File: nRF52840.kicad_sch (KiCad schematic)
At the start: 20 parts, among them J3 JTAG_TC2030, J4 RGB, Q2 2N7002, Q3 AO3407, SW29 RESET, U4 MS88SF3

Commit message: feat(pcb): Version 0.3.1
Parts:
- U4: value MS88SF3 -> (none); footprint Conejo:MS88SF3_PeteJohanson -> (none)
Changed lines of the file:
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@@
     (in_bom yes) (on_board yes)
     (property "Reference" "U4" (id 0) (at 142.875 125.7331 0))
-    (property "Value" "MS88SF3" (id 1) (at 142.875 128.27 0))
-    (property "Footprint" "Conejo:MS88SF3_PeteJohanson" (id 2) (at 170.815 179.07 0)
+    (property "Value" "" (id 1) (at 142.875 128.27 0))
+    (property "Footprint" "" (id 2) (at 170.815 179.07 0)
       (effects (font (size 1.27 1.27)) hide)
     )
@@
       (effects (font (size 1.27 1.27)) (justify left))
     )
-    (property "Value" "MS88SF3" (id 1) (at 161.29 97.155 0)
+    (property "Value" "" (id 1) (at 161.29 97.155 0)
       (effects (font (size 1.27 1.27)) (justify left))
     )
-    (property "Footprint" "Conejo:MS88SF3_PeteJohanson" (id 2) (at 170.815 100.33 0)
+    (property "Footprint" "" (id 2) (at 170.815 100.33 0)
       (effects (font (size 1.27 1.27)) hide)
     )

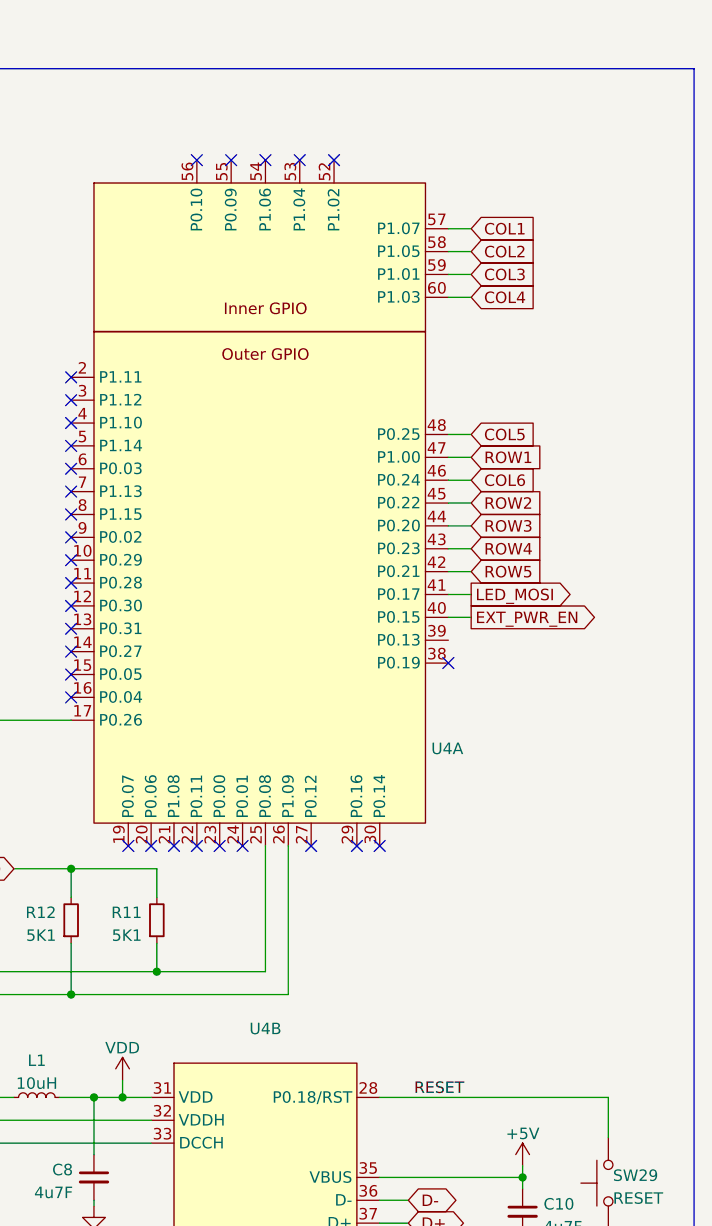
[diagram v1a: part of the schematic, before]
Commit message: feat(pcb): Version 0.3.2
- Move TC2030 footprint to accessible location
- Move diodes to be outside of 14mmx14mm switch area
- Update BOM to remove footprints that don't require placement
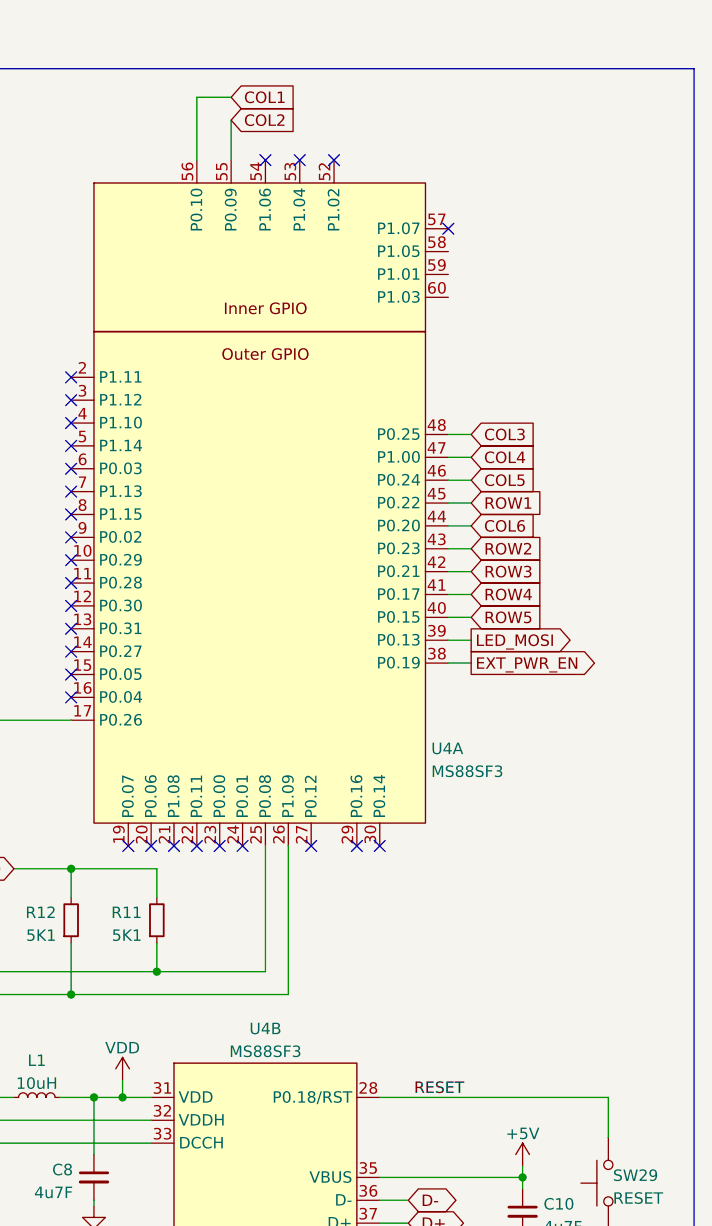
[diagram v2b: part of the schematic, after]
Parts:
- U4: value (none) -> MS88SF3; footprint (none) -> Conejo:MS88SF3_V2
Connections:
- net COL1: now also U4.56 (P0.10); no longer U4.57 (P1.07)
- net COL2: now also U4.55 (P0.09); no longer U4.58 (P1.05)
- net COL3: now also U4.48 (P0.25); no longer U4.59 (P1.01)
- net COL4: now also U4.47 (P1.00); no longer U4.60 (P1.03)
- net COL5: now also U4.46 (P0.24); no longer U4.48 (P0.25)
- net COL6: now also U4.44 (P0.20); no longer U4.46 (P0.24)
- net EXT_PWR_EN: now also U4.38 (P0.19); no longer U4.40 (P0.15)
- net LED_MOSI: now also U4.39 (P0.13); no longer U4.41 (P0.17)
- net ROW1: now also U4.45 (P0.22); no longer U4.47 (P1.00)
- net ROW2: now also U4.43 (P0.23); no longer U4.45 (P0.22)
- net ROW3: now also U4.42 (P0.21); no longer U4.44 (P0.20)
- net ROW4: now also U4.41 (P0.17); no longer U4.43 (P0.23)
- net ROW5: now also U4.40 (P0.15); no longer U4.42 (P0.21)
- no-connect marks 31 -> 29

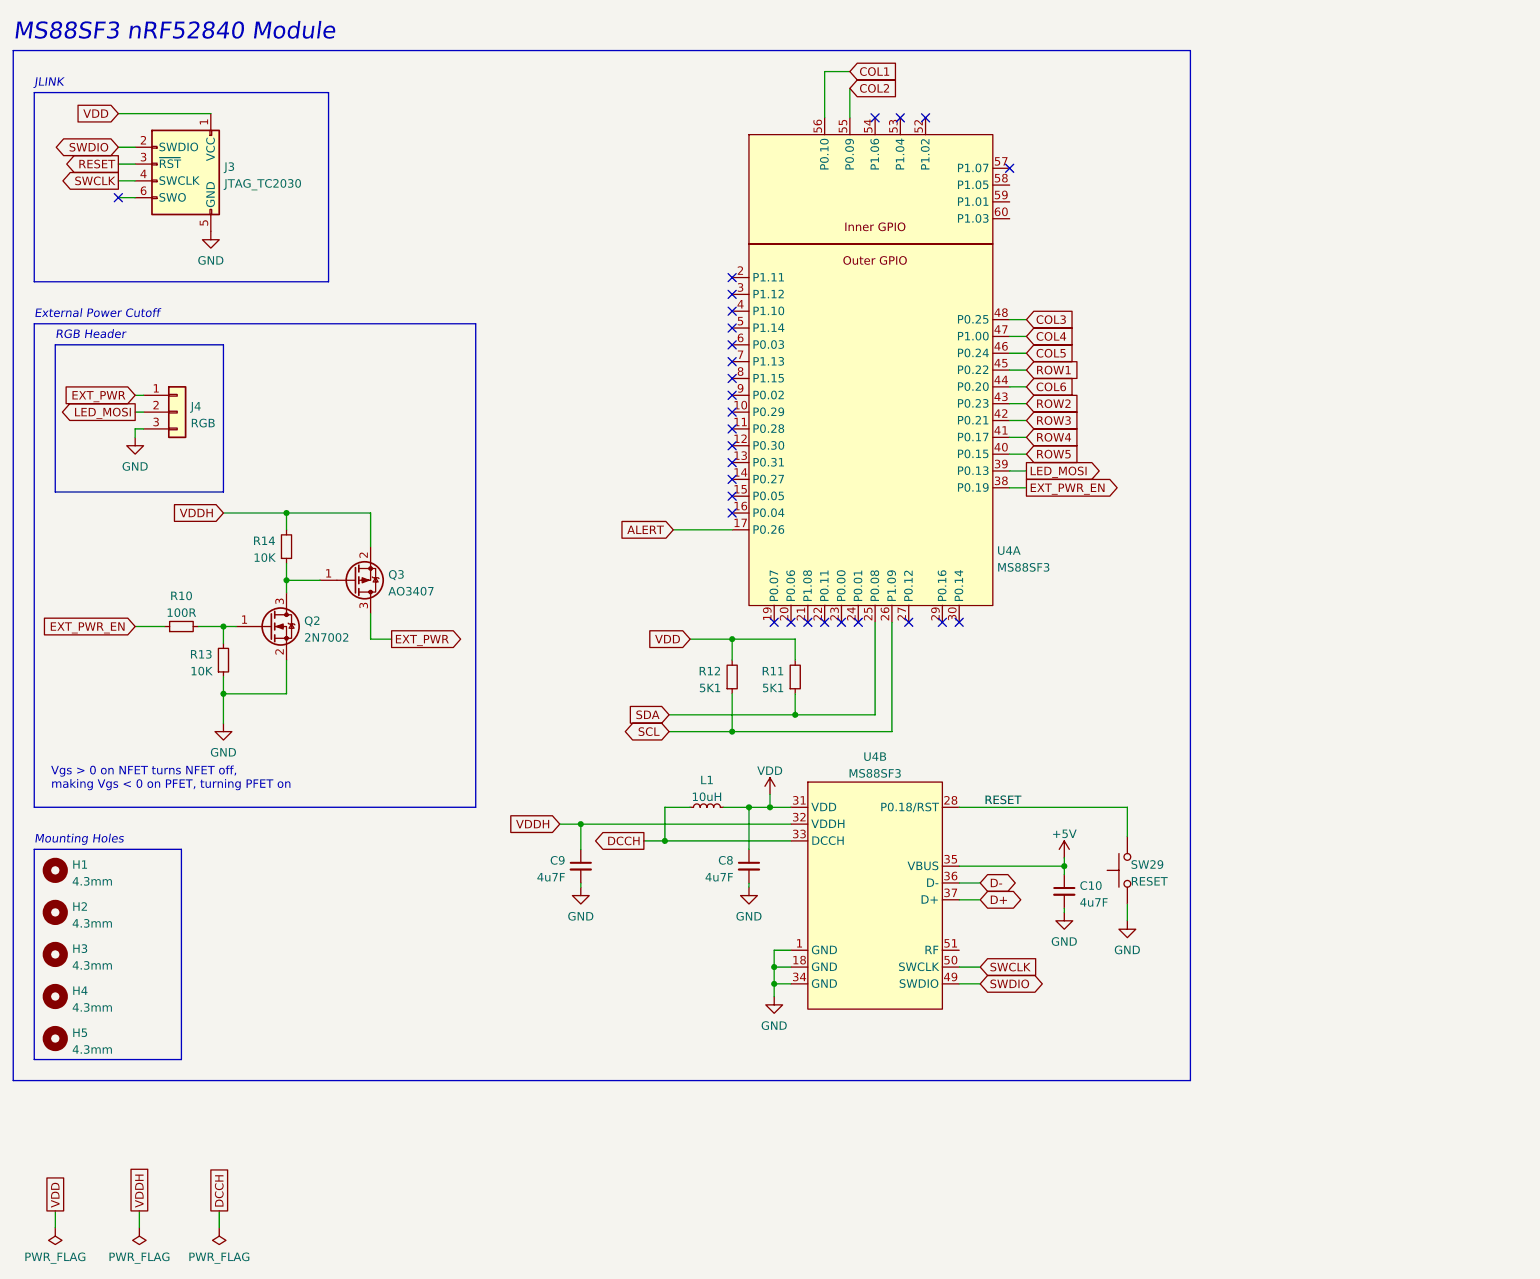
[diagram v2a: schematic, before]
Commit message: feat(schematic): Add titles and individual sheet comments
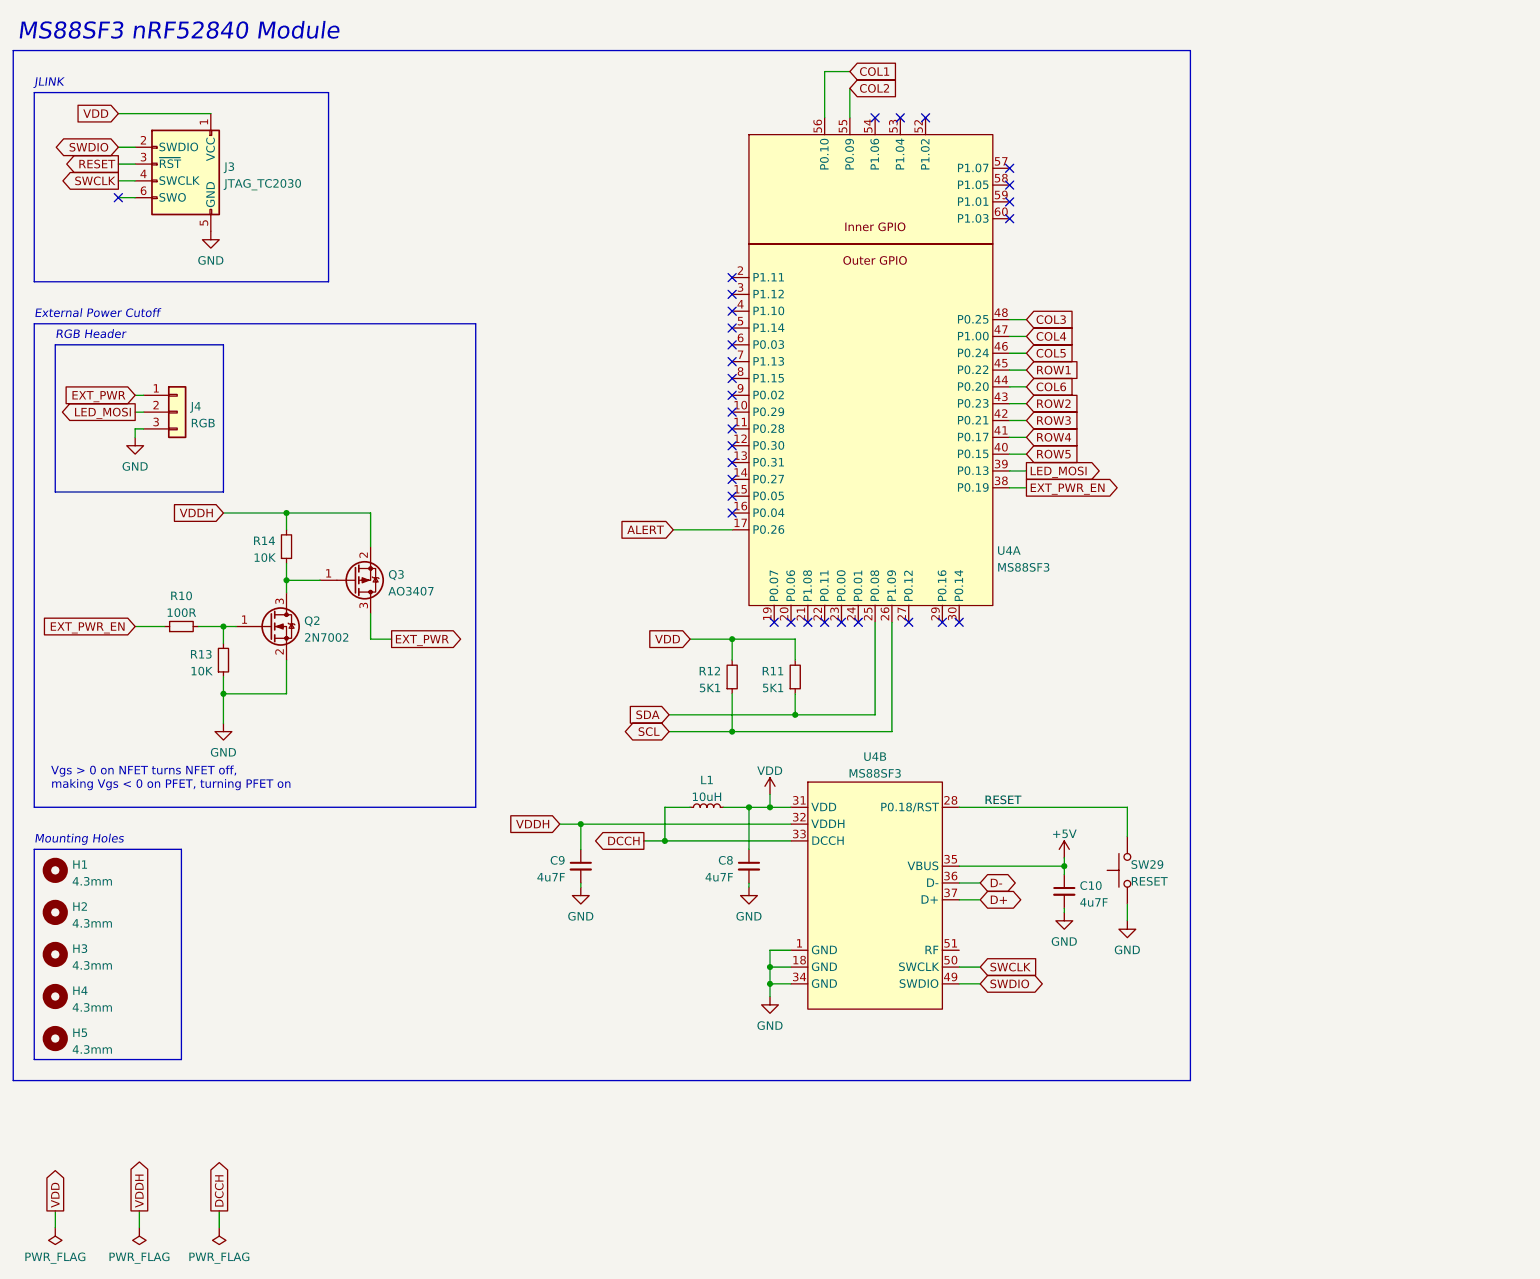
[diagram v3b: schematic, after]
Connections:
- no-connect marks 29 -> 32
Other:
- company: (none) -> Kurtis Lew
- title: (none) -> Conejo nRF52840 Keyboard - nRF52840 Module
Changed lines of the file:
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@@
 (kicad_sch (version 20211123) (generator eeschema)
   (paper "USLetter")
+  (title_block
+    (title "Conejo nRF52840 Keyboard - nRF52840 Module")
+    (company "Kurtis Lew")
+  )
   (junction (at 111.125 138.43) (diameter 0) (color 0 0 0 0)
   )
@@
   (junction (at 121.285 107.95) (diameter 0) (color 0 0 0 0)
   )
-  (junction (at 127.635 157.48) (diameter 0) (color 0 0 0 0)
+  (junction (at 127 157.48) (diameter 0) (color 0 0 0 0)
   )
   (junction (at 123.825 133.35) (diameter 0) (color 0 0 0 0)
@@
   (junction (at 127 133.35) (diameter 0) (color 0 0 0 0)
   )
-  (junction (at 127.635 160.02) (diameter 0) (color 0 0 0 0)
+  (junction (at 127 160.02) (diameter 0) (color 0 0 0 0)
   )
   (junction (at 121.285 121.92) (diameter 0) (color 0 0 0 0)
@@
   (junction (at 98.425 135.89) (diameter 0) (color 0 0 0 0)
   )
+  (no_connect (at 163.195 44.45))
   (no_connect (at 140.335 105.41))
   (no_connect (at 132.715 105.41))
@@
   (no_connect (at 121.285 86.36))
   (no_connect (at 121.285 88.9))
+  (no_connect (at 163.195 39.37))
   (no_connect (at 127.635 105.41))
   (no_connect (at 147.955 105.41))
   (no_connect (at 28.575 41.275))
+  (no_connect (at 163.195 41.91))
   (no_connect (at 155.575 105.41))
   (no_connect (at 153.035 105.41))
@@
     (stroke (width 0) (type default) (color 0 0 0 0))
   )
-  (wire (pts (xy 127.635 157.48) (xy 130.175 157.48))
+  (wire (pts (xy 127 157.48) (xy 130.175 157.48))
     (stroke (width 0) (type default) (color 0 0 0 0))
   )
@@
     (stroke (width 0) (type default) (color 0 0 0 0))
   )
-  (wire (pts (xy 127.635 157.48) (xy 127.635 160.02))
+  (wire (pts (xy 127 157.48) (xy 127 160.02))
     (stroke (width 0) (type default) (color 0 0 0 0))
   )
@@
     (stroke (width 0) (type default) (color 0 0 0 0))
   )
-  (wire (pts (xy 127.635 160.02) (xy 130.175 160.02))
+  (wire (pts (xy 127 160.02) (xy 130.175 160.02))
     (stroke (width 0) (type default) (color 0 0 0 0))
   )
@@
     (stroke (width 0) (type default) (color 0 0 0 0))
   )
-  (wire (pts (xy 127.635 161.925) (xy 127.635 160.02))
-    (stroke (width 0) (type default) (color 0 0 0 0))
-  )
-  (wire (pts (xy 127.635 154.94) (xy 127.635 157.48))
+  (wire (pts (xy 127 161.925) (xy 127 160.02))
+    (stroke (width 0) (type default) (color 0 0 0 0))
+  )
+  (wire (pts (xy 127 154.94) (xy 127 157.48))
     (stroke (width 0) (type default) (color 0 0 0 0))
   )
@@
     (stroke (width 0) (type default) (color 0 0 0 0))
   )
-  (wire (pts (xy 127.635 154.94) (xy 130.175 154.94))
+  (wire (pts (xy 127 154.94) (xy 130.175 154.94))
     (stroke (width 0) (type default) (color 0 0 0 0))
   )
@@
     (effects (font (size 1.27 1.27) italic) (justify left bottom))
   )
-  (text "MS88SF3 nRF52840 Module" (at 12.7 17.78 0)
+  (text "MS88SF3 nRF52840 Module" (at 13.335 17.78 0)
     (effects (font (size 2.54 2.54) italic) (justify left bottom))
   )
@@
     )
   )
-  (global_label "VDDH" (shape passive) (at 31.75 194.31 90) (fields_autoplaced)
+  (global_label "VDDH" (shape output) (at 31.75 194.31 90) (fields_autoplaced)
     (effects (font (size 1.27 1.27)) (justify left))
     (property "Intersheet References" "${INTERSHEET_REFS}" (id 0) (at 31.6706 186.9379 90)
@@
     )
   )
-  (global_label "DCCH" (shape passive) (at 43.815 194.31 90) (fields_autoplaced)
+  (global_label "DCCH" (shape output) (at 43.815 194.31 90) (fields_autoplaced)
     (effects (font (size 1.27 1.27)) (justify left))
     (property "Intersheet References" "${INTERSHEET_REFS}" (id 0) (at 43.7356 186.7564 90)
@@
     )
   )
-  (global_label "VDD" (shape passive) (at 19.05 194.31 90) (fields_autoplaced)
+  (global_label "VDD" (shape output) (at 19.05 194.31 90) (fields_autoplaced)
     (effects (font (size 1.27 1.27)) (justify left))
     (property "Intersheet References" "${INTERSHEET_REFS}" (id 0) (at 18.9706 188.2683 90)
@@
     (pin "2")
   )
-  (symbol (lib_id "power:GND") (at 127.635 161.925 0) (unit 1)
-    (in_bom yes) (on_board yes)
-    (property "Reference" "#PWR0119" (id 0) (at 127.635 168.275 0)
-      (effects (font (size 1.27 1.27)) hide)
-    )
-    (property "Value" "GND" (id 1) (at 127.635 166.3684 0))
-    (property "Footprint" "" (id 2) (at 127.635 161.925 0)
-      (effects (font (size 1.27 1.27)) hide)
-    )
-    (property "Datasheet" "" (id 3) (at 127.635 161.925 0)
-      (effects (font (size 1.27 1.27)) hide)
-    )
+  (symbol (lib_id "power:GND") (at 127 161.925 0) (unit 1)
+    (in_bom yes) (on_board yes)
+    (property "Reference" "#PWR0119" (id 0) (at 127 168.275 0)
+      (effects (font (size 1.27 1.27)) hide)
+    )
+    (property "Value" "GND" (id 1) (at 127 166.3684 0))
+    (property "Footprint" "" (id 2) (at 127 161.925 0)
+      (effects (font (size 1.27 1.27)) hide)
+    )
+    (property "Datasheet" "" (id 3) (at 127 161.925 0)
+      (effects (font (size 1.27 1.27)) hide)
+    )
